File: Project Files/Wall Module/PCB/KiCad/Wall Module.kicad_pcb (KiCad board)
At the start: 2 copper layers, 48.5 x 54.4 mm, 15 parts, among them J1 Conn_02x03_Top_Bottom (C65114), J2 Screw_Terminal_01x04 (C280261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, K1 SANYOU_SRD_Form_C (C35449), K2 SANYOU_SRD_Form_C (C35449), Q1 MMBT3904 (C20526), Q2 MMBT3904 (C20526), U1 AMS1117-3.3 (C173386)

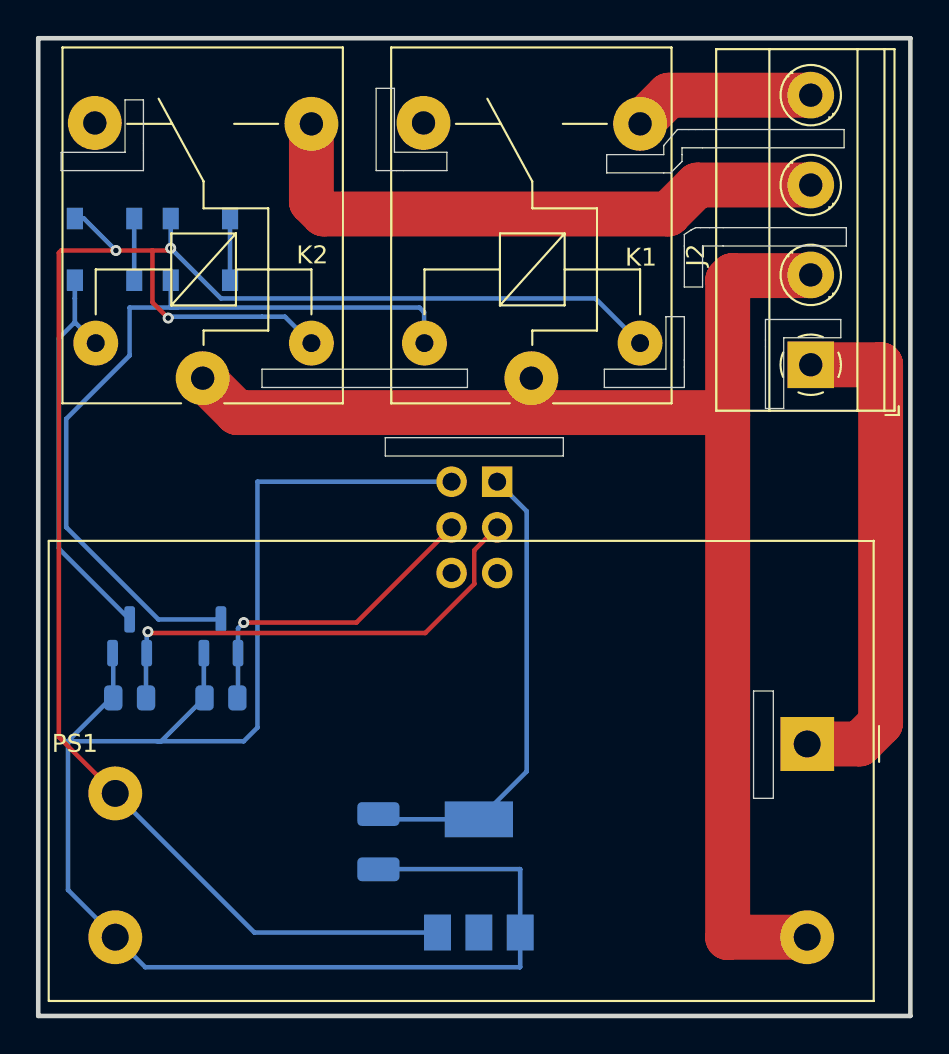
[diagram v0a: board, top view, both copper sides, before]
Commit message: Made screen module pcb.
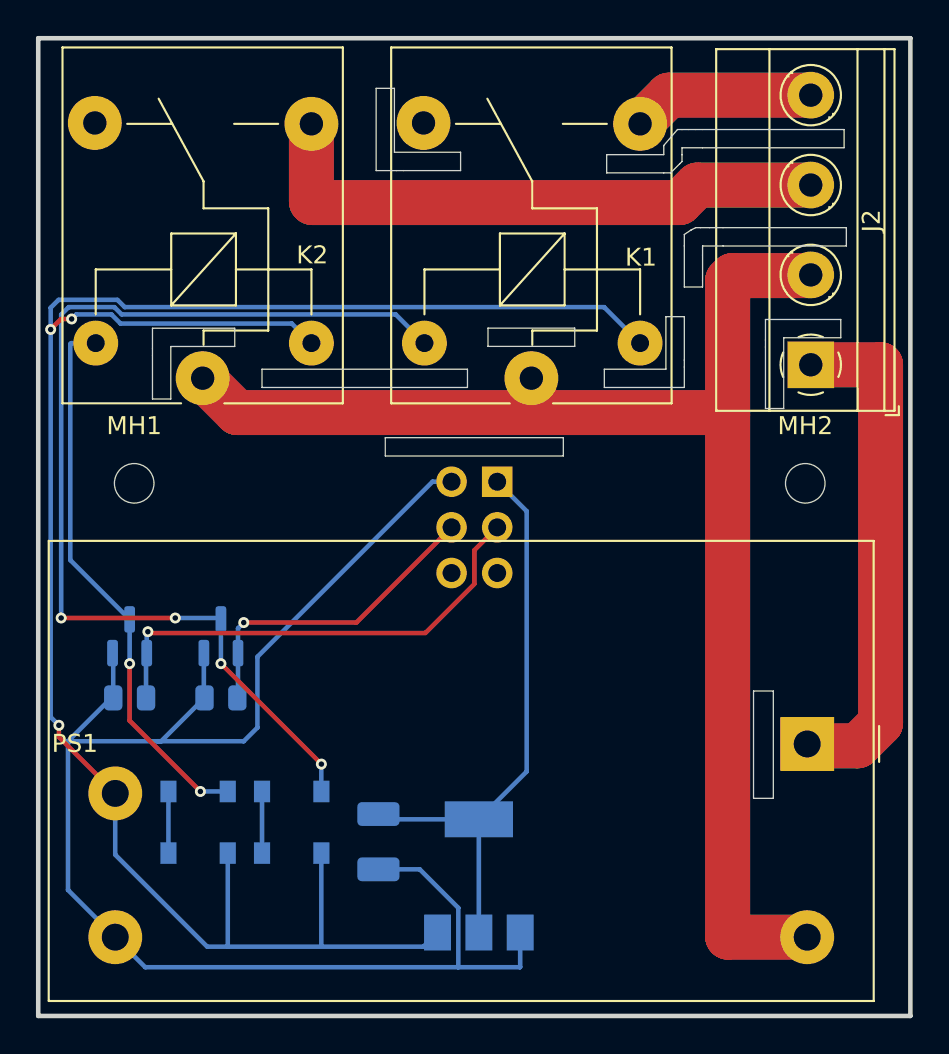
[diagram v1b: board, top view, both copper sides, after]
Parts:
- added MH1: MountingHole_2.2mm_M2, MountingHole:MountingHole_2.2mm_M2, F.Cu at (164.2, 94.6)
- added MH2: MountingHole_2.2mm_M2, MountingHole:MountingHole_2.2mm_M2, F.Cu at (201.5, 94.6)
- moved D3 35.7 mm to (167.8, 115.2), turned to 180 degrees
- moved D1 35.7 mm to (173.0, 115.2), turned to 180 degrees
- moved D4 28.9 mm to (167.8, 111.8), turned to 180 degrees
- moved D2 28.9 mm to (173.0, 111.8), turned to 180 degrees
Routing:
- net L: track 77.8 -> 155.4 mm
- net RELAY1: track 33.1 -> 65.1 mm
- net N: track 28.4 -> 56.9 mm
- net Net-(D2-Pad1): track 44.5 -> 58.9 mm, vias 0 -> 4
- net RELAY2: track 10.2 -> 20.3 mm
- net GND: track 96.1 -> 87.6 mm
- net Net-(D4-Pad1): track 22.5 -> 30.9 mm, vias 0 -> 2
- net 5V: track 104.6 -> 112.1 mm
- net 3.3V: track 26.3 -> 32.6 mm
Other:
- outline, holes or cut-outs redrawn

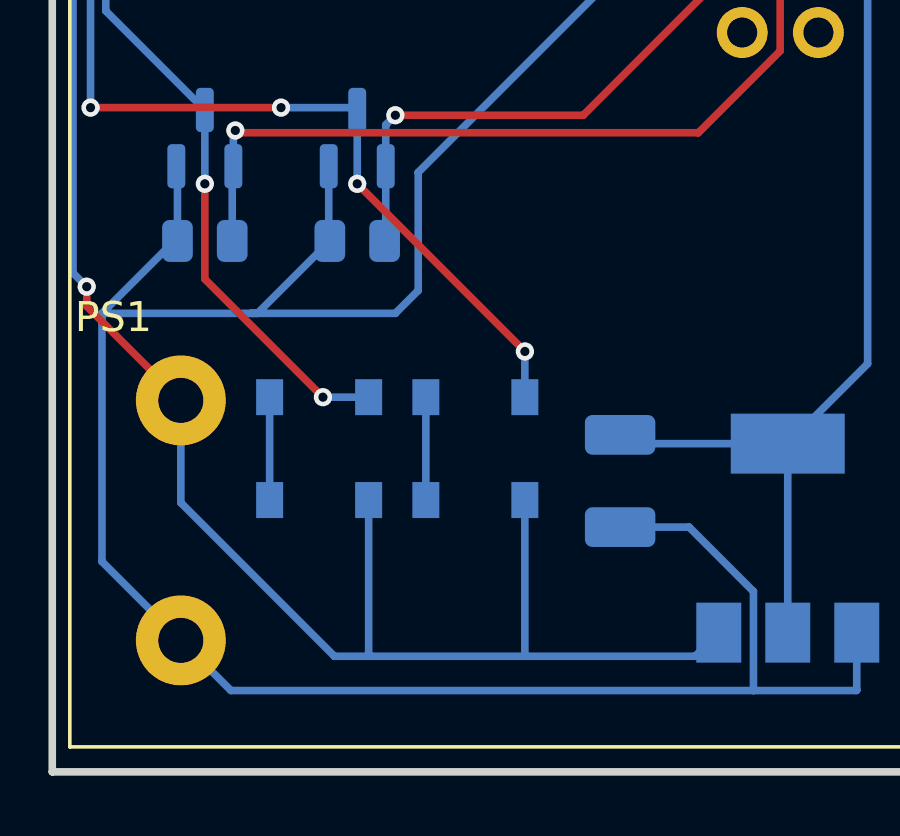
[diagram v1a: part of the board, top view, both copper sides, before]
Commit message: Updated PCB to fix several issues Wall Module: Fixed relay flyback diodes pointing in the wrong direction.
Screen PCB:
Fixed display LED resistors to be a more suitable value.
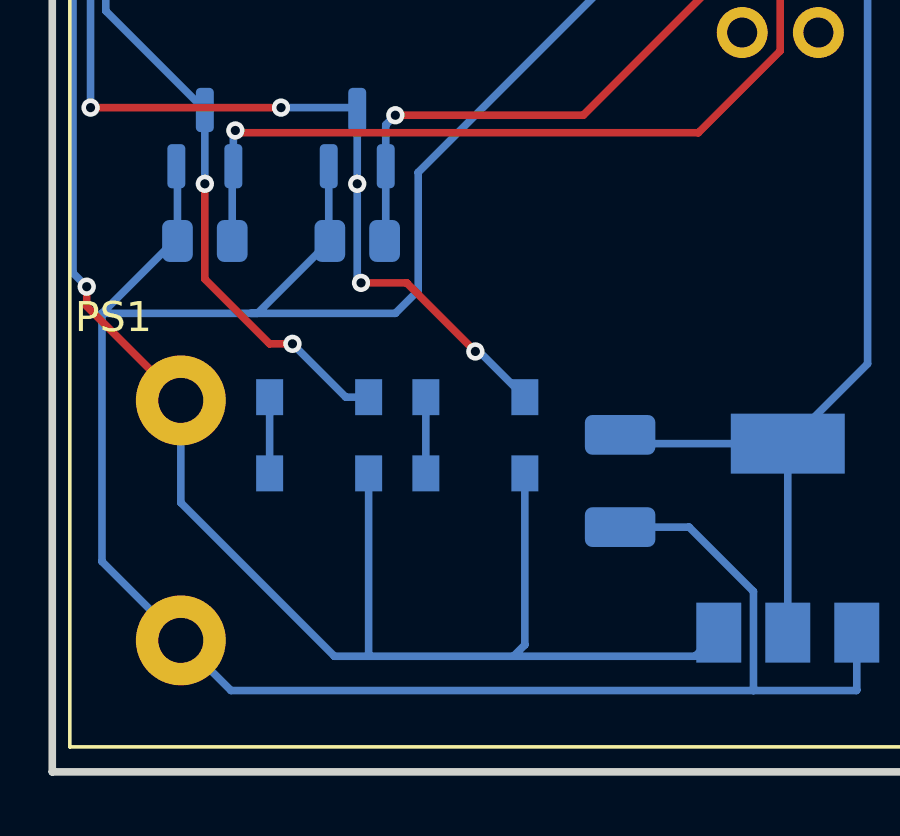
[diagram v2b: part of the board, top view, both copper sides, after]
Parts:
- moved D1 3.43 mm to (173.0, 111.8)
- moved D3 3.43 mm to (167.8, 111.8)
- moved D2 2.54 mm to (173.0, 114.3)
- moved D4 2.54 mm to (167.8, 114.3)
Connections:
- D1 pad 1: 5V -> Net-(D1-Pad1)
- D2 pad 1: Net-(D2-Pad1) -> 5V
- D3 pad 1: 5V -> Net-(D3-Pad1)
- D4 pad 1: Net-(D4-Pad1) -> 5V
- K1 pad 5: Net-(D2-Pad1) -> Net-(D1-Pad1)
- K2 pad 5: Net-(D4-Pad1) -> Net-(D3-Pad1)
- Q1 pad 3: Net-(D2-Pad1) -> Net-(D1-Pad1)
- Q2 pad 3: Net-(D4-Pad1) -> Net-(D3-Pad1)
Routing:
- net Net-(D1-Pad1): track 0.00 -> 59.9 mm, vias 0 -> 5
- net Net-(D2-Pad1): track 58.9 -> 0.00 mm, vias 4 -> 0
- net Net-(D4-Pad1): track 30.9 -> 0.00 mm, vias 2 -> 0
- net Net-(D3-Pad1): track 0.00 -> 30.9 mm, vias 0 -> 2
- net 5V: track 112.1 -> 114.1 mm
- net Net-(D3-Pad2): track 3.43 -> 2.54 mm
- net Net-(D1-Pad2): track 3.43 -> 2.54 mm
